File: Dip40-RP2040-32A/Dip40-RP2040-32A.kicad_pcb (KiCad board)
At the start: 2 copper layers, 18.5 x 51.6 mm, 30 parts, among them J2 SKRKAEE020, J3 2.54mm header 01x20, J4 2.54mm header 01x20, J5 Conn_01x03_Male, U1 TPS63002, U3 RP2040, X1 XO 32 12Mhz 3225 seiko

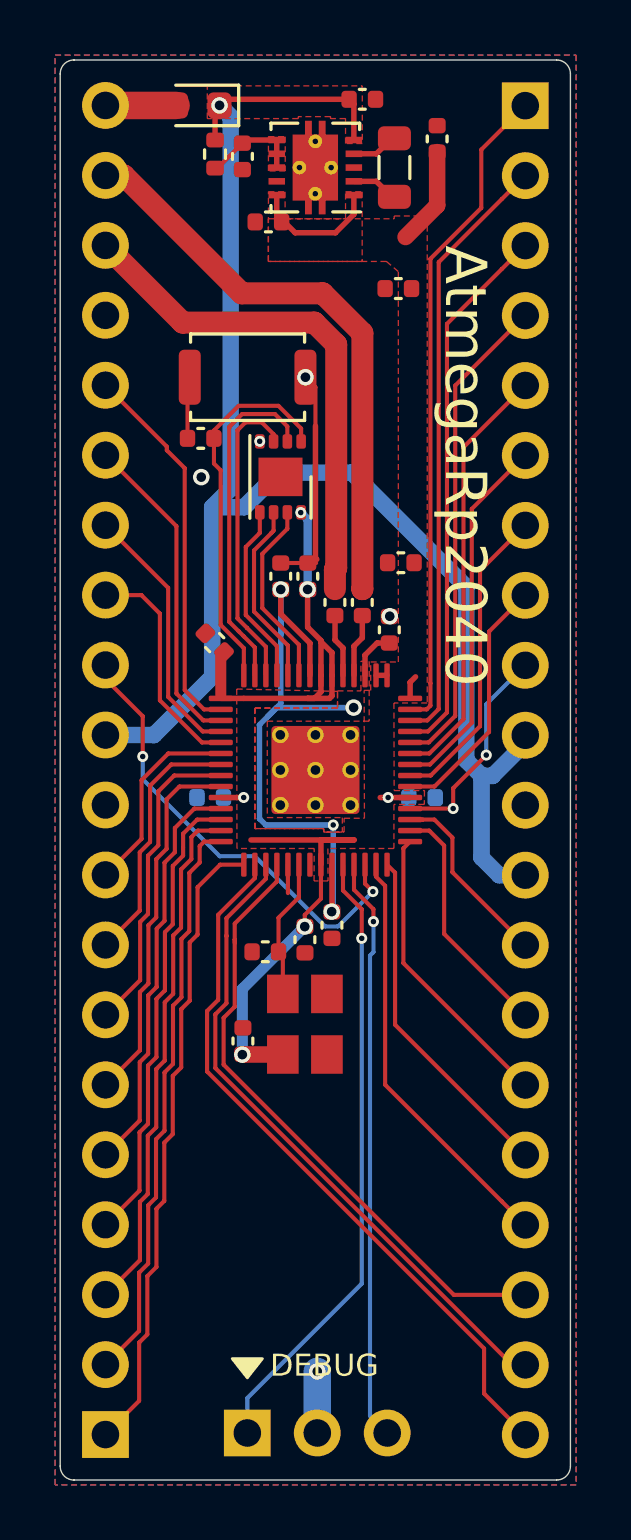
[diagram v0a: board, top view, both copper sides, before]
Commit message: moved some more components to better places.
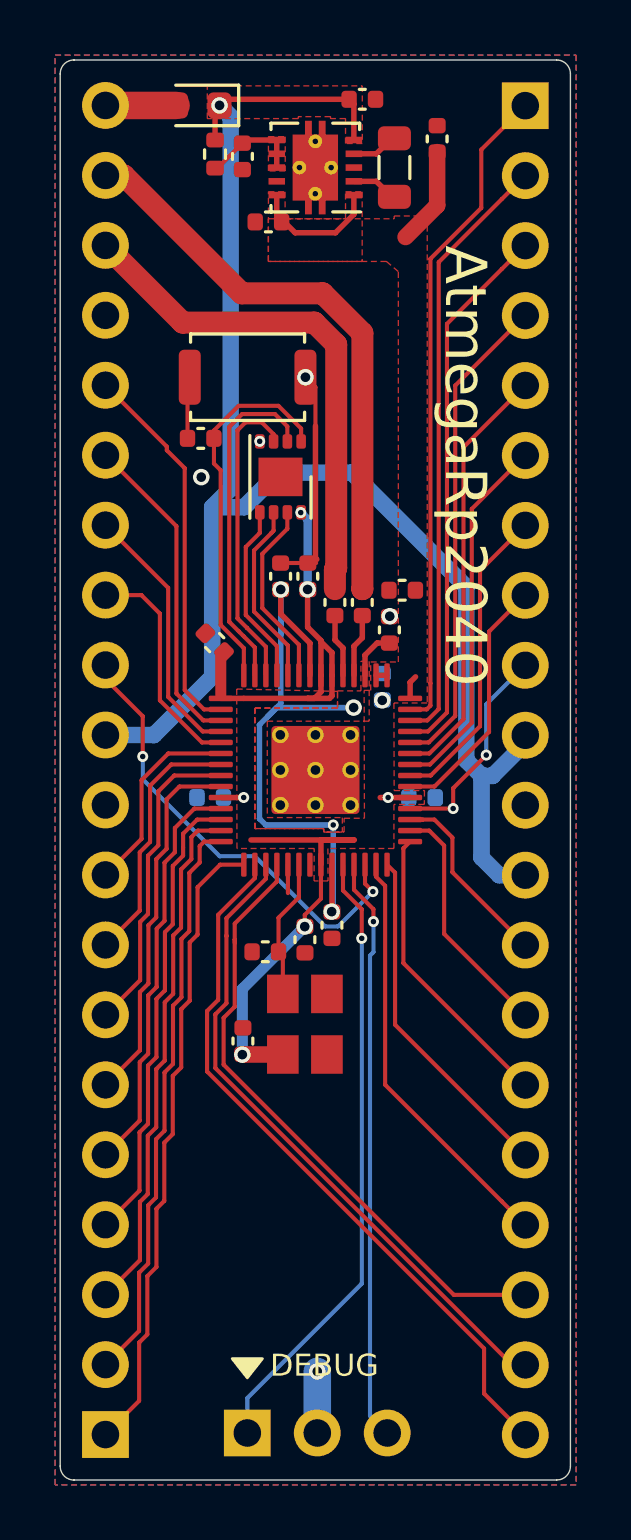
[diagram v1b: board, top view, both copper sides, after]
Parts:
- C10: moved to B.Cu
- moved C10 14.5 mm to (106.1, 79.8), turned to 90 degrees
- moved C6 4.40 mm to (102.4, 75.8)
- moved C3 4.40 mm to (106.3, 77.8)
- moved C8 1.00 mm to (106.8, 76.3)
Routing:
- net +3V3: vias 6 -> 7

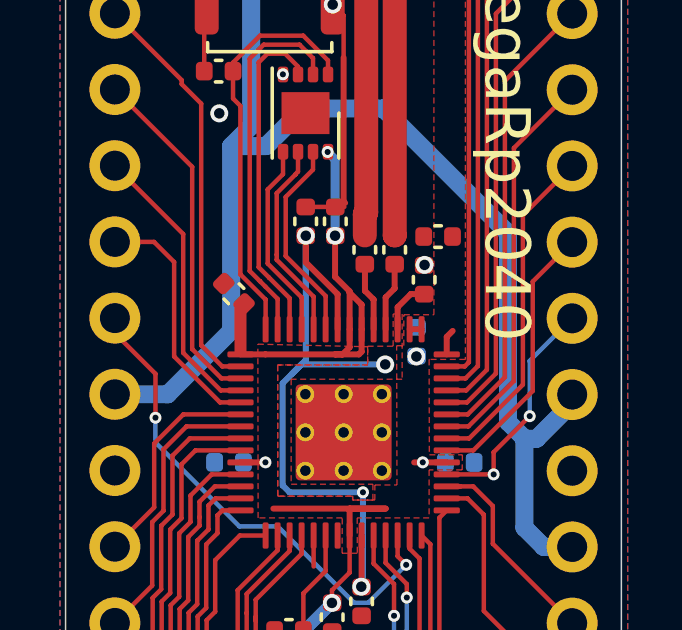
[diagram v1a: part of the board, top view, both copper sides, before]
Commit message: moved C11 on 32A board closer to the MCU
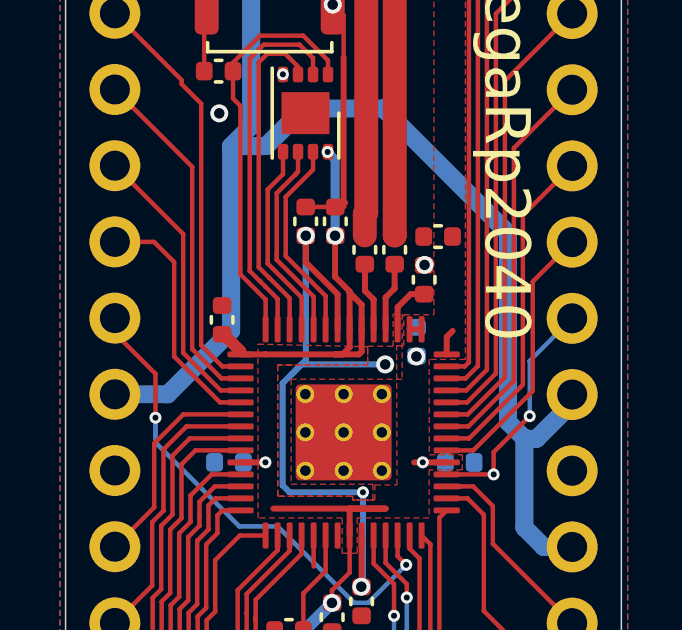
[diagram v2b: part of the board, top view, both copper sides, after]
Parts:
- moved C11 0.96 mm to (99.6, 79.1), turned to 90 degrees
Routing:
- net +3V3: track 44.4 -> 42.9 mm
